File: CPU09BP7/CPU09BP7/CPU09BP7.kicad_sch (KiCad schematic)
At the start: 82 parts, among them J1 ATX-24, J1 BUS-A, J10 C_23, J11 C_23A, J12 C_1A, J13 C_2A, J14 C_29A, J15 C_28A, J16 ACCA, J17 ACCB, J18 A29, J19 A30, J2 +12V, J20 C_1B, J21 C_28B, J22 BCCA, J23 BCCB, J24 BUS-B, J25 C_2B, J26 C_23B, J27 C_29B, J28 B29, J29 B30, J3 -12V, J30 C_1C, J31 C_28C, J32 CCCA, J33 CCCB, J34 BUS-C, J35 C_2C, J36 C_23C, J37 C_29C, J38 C29, J39 C30, J4 3.3V, J40 C_1D, J41 C_28D, J42 DCCA, J43 DCCB, J44 BUS-D, J45 C_2D, J46 C_23D, J47 C_29D, J48 D29, J49 D30, J5 PSON, J50 C_1E, J51 C_28E, J52 ECCA, J53 ECCB, J54 BUS-E, J55 C_2E, J56 C_23E, J57 C_29E, J58 E29, J59 E30, J6 GND, J60 C_1F, J61 C_28F, J62 FCCA, J63 FCCB, J64 BUS-F, J65 C_2F, J66 C_23F, J67 C_29F, J68 F29, J69 F30, J7 GND, J70 C_1G, J71 C_28G, J72 GCCA, J73 GCCB, J74 BUS-G, J75 C_2G, J76 C_23G, J77 C_29G, J78 G29, J79 G30, J8 ~{RES}, J9 ~{RES0}

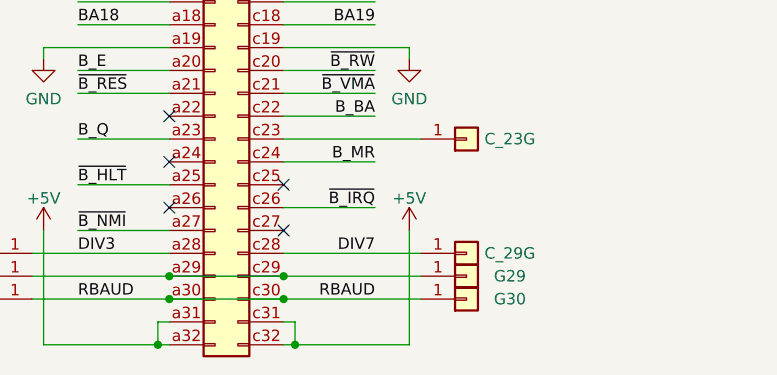
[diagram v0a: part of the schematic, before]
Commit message: Backplane BP7 started with board
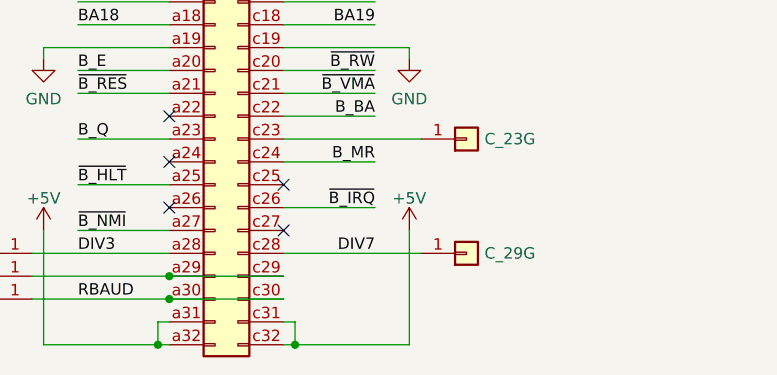
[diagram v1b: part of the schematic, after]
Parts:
- removed J78: G29, symbol Connector_Generic:Conn_01x01
- removed J79: G30, symbol Connector_Generic:Conn_01x01
- D1: footprint (none) -> Diode_THT:D_DO-201AE_P15.24mm_Horizontal
- F1: footprint (none) -> Fuse:Fuseholder_TR5_Littelfuse_No560_No460
- J1: footprint (none) -> Connector_Molex:Molex_Mini-Fit_Jr_5566-24A_2x12_P4.20mm_Vertical
- J1, J24, J34, J44, J54, J64, J74: footprint (none) -> Connector_DIN:DIN41612_C_2x32_Female_Vertical_THT
- J10, J11, J12, J13, J14, J15, J16, J17, J18, J19, J2, J20, J21, J22, J23, J25, J26, J27, J28, J29, J3, J30, J31, J32, J33, J35, J36, J37, J38, J39, J4, J40, J41, J42, J43, J45, J46, J47, J48, J49, J5, J50, J51, J52, J53, J55, J56, J57, J58, J59, J6, J60, J61, J62, J63, J65, J66, J67, J68, J69, J7, J70, J71, J72, J73, J75, J76, J77, J8, J9: footprint (none) -> Connector_PinHeader_2.54mm:PinHeader_1x01_P2.54mm_Vertical

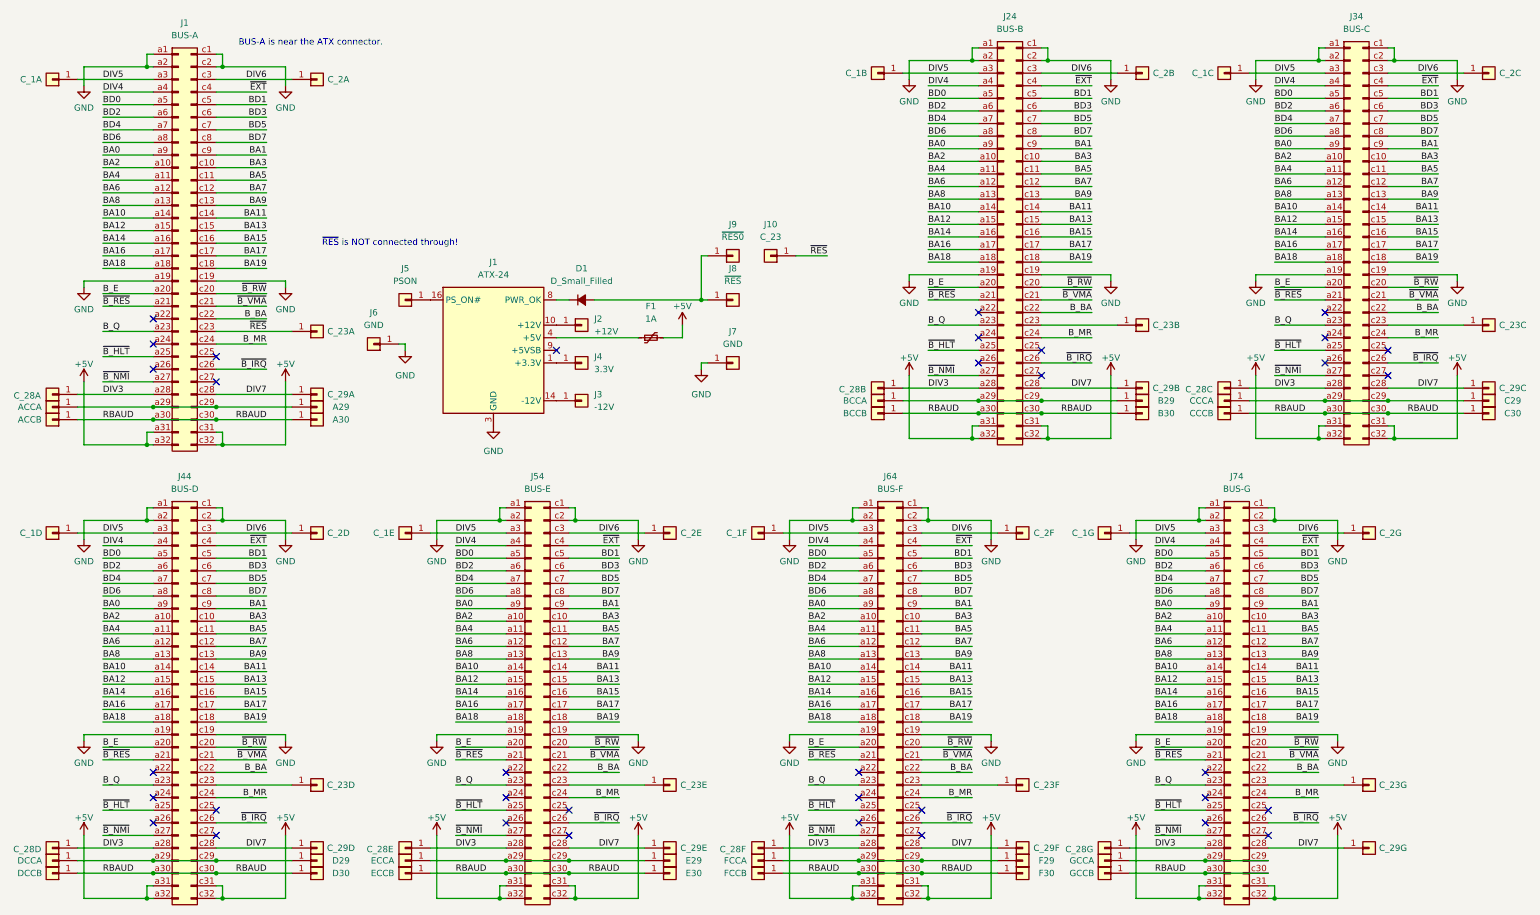
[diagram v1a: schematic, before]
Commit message: Backplane BP7 mostly finished
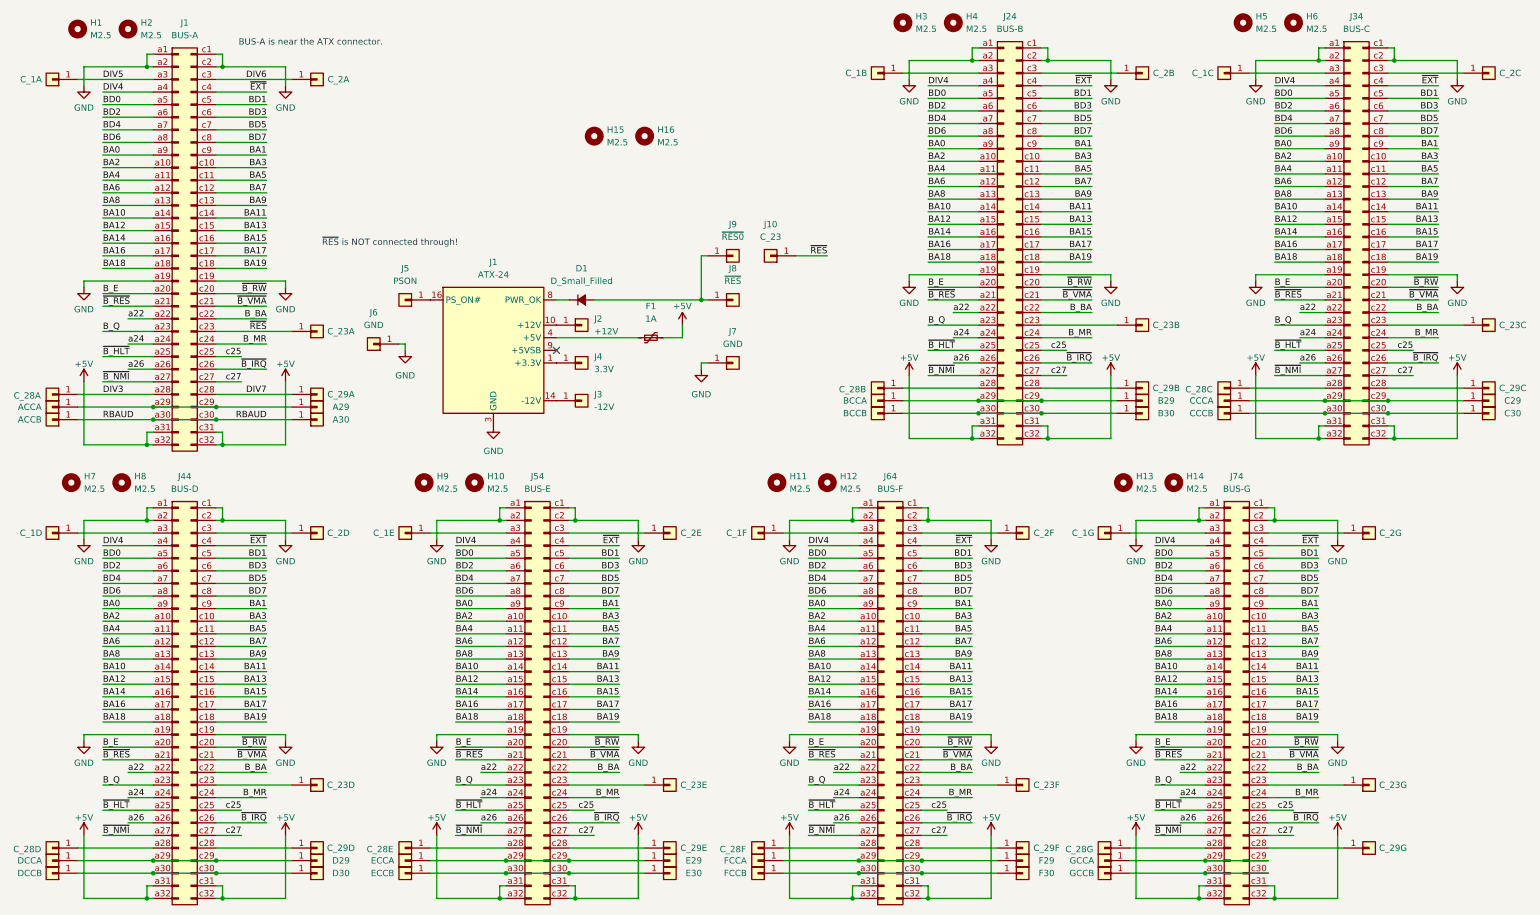
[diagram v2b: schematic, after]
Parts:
- added H1, H10, H11, H12, H13, H14, H15, H16, H2, H3, H4, H5, H6, H7, H8, H9: M2.5, MountingHole:MountingHole_2.5mm, symbol Mechanical:MountingHole
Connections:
- net DIV3: no longer J21.1 (Pin_1), J24.a28 (Pin_a28), J31.1 (Pin_1), J34.a28 (Pin_a28), J41.1 (Pin_1), J44.a28 (Pin_a28), J51.1 (Pin_1), J54.a28 (Pin_a28), J61.1 (Pin_1), J64.a28 (Pin_a28), J71.1 (Pin_1), J74.a28 (Pin_a28)
- net DIV5: no longer J20.1 (Pin_1), J24.a3 (Pin_a3), J30.1 (Pin_1), J34.a3 (Pin_a3), J40.1 (Pin_1), J44.a3 (Pin_a3), J50.1 (Pin_1), J54.a3 (Pin_a3), J60.1 (Pin_1), J64.a3 (Pin_a3), J70.1 (Pin_1), J74.a3 (Pin_a3)
- net DIV6: no longer J24.c3 (Pin_c3), J25.1 (Pin_1), J34.c3 (Pin_c3), J35.1 (Pin_1), J44.c3 (Pin_c3), J45.1 (Pin_1), J54.c3 (Pin_c3), J55.1 (Pin_1), J64.c3 (Pin_c3), J65.1 (Pin_1), J74.c3 (Pin_c3), J75.1 (Pin_1)
- net DIV7: no longer J24.c28 (Pin_c28), J27.1 (Pin_1), J34.c28 (Pin_c28), J37.1 (Pin_1), J44.c28 (Pin_c28), J47.1 (Pin_1), J54.c28 (Pin_c28), J57.1 (Pin_1), J64.c28 (Pin_c28), J67.1 (Pin_1), J74.c28 (Pin_c28), J77.1 (Pin_1)
- net RBAUD: no longer J23.1 (Pin_1), J24.a30 (Pin_a30), J24.c30 (Pin_c30), J29.1 (Pin_1), J33.1 (Pin_1), J34.a30 (Pin_a30), J34.c30 (Pin_c30), J39.1 (Pin_1), J43.1 (Pin_1), J44.a30 (Pin_a30), J44.c30 (Pin_c30), J49.1 (Pin_1), J53.1 (Pin_1), J54.a30 (Pin_a30), J54.c30 (Pin_c30), J59.1 (Pin_1), J63.1 (Pin_1), J64.a30 (Pin_a30), J64.c30 (Pin_c30), J69.1 (Pin_1), J73.1 (Pin_1), J74.a30 (Pin_a30), J74.c30 (Pin_c30)
- net a22: now reaches J24.a22 (Pin_a22)
- net a22: now also J1.a22 (Pin_a22), J34.a22 (Pin_a22), J44.a22 (Pin_a22), J54.a22 (Pin_a22), J64.a22 (Pin_a22), J74.a22 (Pin_a22)
- net a24: now reaches J24.a24 (Pin_a24)
- net a24: now also J1.a24 (Pin_a24), J34.a24 (Pin_a24), J44.a24 (Pin_a24), J54.a24 (Pin_a24), J64.a24 (Pin_a24), J74.a24 (Pin_a24)
- net a26: now reaches J24.a26 (Pin_a26)
- net a26: now also J1.a26 (Pin_a26), J34.a26 (Pin_a26), J44.a26 (Pin_a26), J54.a26 (Pin_a26), J64.a26 (Pin_a26), J74.a26 (Pin_a26)
- net c25: now reaches J24.c25 (Pin_c25)
- net c25: now also J1.c25 (Pin_c25), J34.c25 (Pin_c25), J44.c25 (Pin_c25), J54.c25 (Pin_c25), J64.c25 (Pin_c25), J74.c25 (Pin_c25)
- net c27: now reaches J24.c27 (Pin_c27)
- net c27: now also J1.c27 (Pin_c27), J34.c27 (Pin_c27), J44.c27 (Pin_c27), J54.c27 (Pin_c27), J64.c27 (Pin_c27), J74.c27 (Pin_c27)
- new net: J21.1 (Pin_1), J24.a28 (Pin_a28)
- new net: J20.1 (Pin_1), J24.a3 (Pin_a3)
- new net: J23.1 (Pin_1), J24.a30 (Pin_a30), J24.c30 (Pin_c30), J29.1 (Pin_1)
- new net: J24.c28 (Pin_c28), J27.1 (Pin_1)
- new net: J24.c3 (Pin_c3), J25.1 (Pin_1)
- new net: J31.1 (Pin_1), J34.a28 (Pin_a28)
- new net: J30.1 (Pin_1), J34.a3 (Pin_a3)
- new net: J33.1 (Pin_1), J34.a30 (Pin_a30), J34.c30 (Pin_c30), J39.1 (Pin_1)
- new net: J34.c28 (Pin_c28), J37.1 (Pin_1)
- new net: J34.c3 (Pin_c3), J35.1 (Pin_1)
- new net: J71.1 (Pin_1), J74.a28 (Pin_a28)
- new net: J70.1 (Pin_1), J74.a3 (Pin_a3)
- new net: J73.1 (Pin_1), J74.a30 (Pin_a30), J74.c30 (Pin_c30)
- new net: J74.c28 (Pin_c28), J77.1 (Pin_1)
- new net: J74.c3 (Pin_c3), J75.1 (Pin_1)
- new net: J51.1 (Pin_1), J54.a28 (Pin_a28)
- new net: J44.c3 (Pin_c3), J45.1 (Pin_1)
- new net: J41.1 (Pin_1), J44.a28 (Pin_a28)
- new net: J40.1 (Pin_1), J44.a3 (Pin_a3)
- new net: J43.1 (Pin_1), J44.a30 (Pin_a30), J44.c30 (Pin_c30), J49.1 (Pin_1)
- new net: J44.c28 (Pin_c28), J47.1 (Pin_1)
- new net: J60.1 (Pin_1), J64.a3 (Pin_a3)
- new net: J50.1 (Pin_1), J54.a3 (Pin_a3)
- new net: J64.c3 (Pin_c3), J65.1 (Pin_1)
- new net: J53.1 (Pin_1), J54.a30 (Pin_a30), J54.c30 (Pin_c30), J59.1 (Pin_1)
- new net: J63.1 (Pin_1), J64.a30 (Pin_a30), J64.c30 (Pin_c30), J69.1 (Pin_1)
- new net: J54.c28 (Pin_c28), J57.1 (Pin_1)
- new net: J61.1 (Pin_1), J64.a28 (Pin_a28)
- new net: J64.c28 (Pin_c28), J67.1 (Pin_1)
- new net: J54.c3 (Pin_c3), J55.1 (Pin_1)
- no-connect marks 36 -> 1
